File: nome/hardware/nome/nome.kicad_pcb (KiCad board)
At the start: 2 copper layers, 91.4 x 91.4 mm, 63 parts, among them J1 SJ-2524, J2 JTAG_SWD, J3 JST, J4 7SEG_DEBUG, SW1 SW_SPDT, SW2 Rotary_Encoder_Switch, U1 LM1117-1.8, U2 LM1117-3.3, U3 AS1115, U4 STMF411CEU6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

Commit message: Add metronome logo
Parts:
- added G***: LOGO, nome:metronome_logo, F.Cu at (90.4, 55.9)
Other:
- board text added: "NOME"
- board text added: "rev. A"
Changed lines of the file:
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@@
 (general
   (thickness 1.6)
-  (drawings 8)
+  (drawings 10)
   (tracks 937)
   (zones 0)
-  (modules 63)
+  (modules 64)
   (nets 107)
 )
@@
   (add_net +3V3)
 )
+  (module nome:metronome_logo (layer F.Cu)
+    (at 90.424 55.88)
+    (fp_text reference G*** (at 0 0) (layer F.SilkS) hide
+      (effects (font (thickness 0.3)))
+    )
+    (fp_text value LOGO (at 0.75 0) (layer F.SilkS) hide
+      (effects (font (thickness 0.3)))
+    )
+    (fp_poly (pts (xy 0.299212 -0.292148) (xy 0.233636 -0.169677) (xy 0.185654 -0.087032) (xy 0.149307 -0.036532)
+      (xy 0.118634 -0.010493) (xy 0.087674 -0.001233) (xy 0.072913 -0.000498) (xy 0 0)
+      (xy 0 -0.583298) (xy 0.452599 -0.583298) (xy 0.299212 -0.292148)) (layer F.SilkS) (width 0.01))
+    (fp_poly (pts (xy 2.59313 -0.961869) (xy 2.608985 -0.892796) (xy 2.630901 -0.784862) (xy 2.657712 -0.644817)
+      (xy 2.68825 -0.47941) (xy 2.721348 -0.295389) (xy 2.755838 -0.099504) (xy 2.790553 0.101496)
+      (xy 2.824326 0.300863) (xy 2.855989 0.491847) (xy 2.884375 0.667699) (xy 2.908317 0.821671)
+      (xy 2.926647 0.947014) (xy 2.938198 1.036978) (xy 2.941811 1.080428) (xy 2.943007 1.140084)
+      (xy 2.184533 1.140084) (xy 1.955859 1.139619) (xy 1.775596 1.138089) (xy 1.639137 1.135287)
+      (xy 1.541874 1.131009) (xy 1.479199 1.125051) (xy 1.446503 1.117207) (xy 1.439179 1.107272)
+      (xy 1.439302 1.106942) (xy 1.459766 1.06404) (xy 1.50165 0.982744) (xy 1.561826 0.86877)
+      (xy 1.637164 0.727837) (xy 1.724535 0.565661) (xy 1.820809 0.387959) (xy 1.922858 0.200449)
+      (xy 2.027552 0.008848) (xy 2.131761 -0.181127) (xy 2.232356 -0.363758) (xy 2.326208 -0.533328)
+      (xy 2.410188 -0.684121) (xy 2.481167 -0.810418) (xy 2.536014 -0.906502) (xy 2.5716 -0.966657)
+      (xy 2.584504 -0.985334) (xy 2.59313 -0.961869)) (layer F.SilkS) (width 0.01))
+    (fp_poly (pts (xy 0.615084 -6.781882) (xy 0.871614 -6.781131) (xy 1.099834 -6.779907) (xy 1.295607 -6.778237)
+      (xy 1.454793 -6.77615) (xy 1.573254 -6.773674) (xy 1.646851 -6.770837) (xy 1.671462 -6.767759)
+      (xy 1.675862 -6.738117) (xy 1.687978 -6.661689) (xy 1.706912 -6.544009) (xy 1.731765 -6.390615)
+      (xy 1.76164 -6.207041) (xy 1.795638 -5.998825) (xy 1.832862 -5.771502) (xy 1.853025 -5.648616)
+      (xy 1.89866 -5.36869) (xy 1.935741 -5.136227) (xy 1.964883 -4.946459) (xy 1.986699 -4.794621)
+      (xy 2.001804 -4.675946) (xy 2.010813 -4.585669) (xy 2.01434 -4.519022) (xy 2.013001 -4.471241)
+      (xy 2.008577 -4.442249) (xy 1.99512 -4.321577) (xy 1.999644 -4.171198) (xy 2.020312 -4.010591)
+      (xy 2.055292 -3.859236) (xy 2.066938 -3.822526) (xy 2.118092 -3.672129) (xy 1.362154 -2.26691)
+      (xy 1.226216 -2.014549) (xy 1.097316 -1.775905) (xy 0.977708 -1.555108) (xy 0.869648 -1.35629)
+      (xy 0.77539 -1.183582) (xy 0.697188 -1.041115) (xy 0.637298 -0.93302) (xy 0.597973 -0.863427)
+      (xy 0.581501 -0.836503) (xy 0.567022 -0.844537) (xy 0.55856 -0.899949) (xy 0.556785 -0.962442)
+      (xy 0.556785 -1.11357) (xy 0 -1.11357) (xy 0 -1.696868) (xy 0.556785 -1.696868)
+      (xy 0.556785 -2.253653) (xy 0 -2.253653) (xy 0 -2.836952) (xy 0.556785 -2.836952)
+      (xy 0.556785 -3.393737) (xy 0 -3.393737) (xy 0 -3.977035) (xy 0.556785 -3.977035)
+      (xy 0.556785 -4.507306) (xy 0 -4.507306) (xy 0 -5.090605) (xy 0.556785 -5.090605)
+      (xy 0.556785 -5.64739) (xy -1.11357 -5.64739) (xy -1.11357 -5.090605) (xy -0.556785 -5.090605)
+      (xy -0.556785 -4.507306) (xy -1.11357 -4.507306) (xy -1.11357 -3.977035) (xy -0.556785 -3.977035)
+      (xy -0.556785 -3.393737) (xy -1.11357 -3.393737) (xy -1.11357 -2.836952) (xy -0.556785 -2.836952)
+      (xy -0.556785 -2.253653) (xy -1.11357 -2.253653) (xy -1.11357 -1.696868) (xy -0.556785 -1.696868)
+      (xy -0.556785 -1.11357) (xy -1.11357 -1.11357) (xy -1.11357 -0.583298) (xy -0.556785 -0.583298)
+      (xy -0.556785 0) (xy -1.11357 0) (xy -1.11357 0.556785) (xy -0.556785 0.556785)
+      (xy -0.556785 1.140084) (xy -2.041544 1.140084) (xy -2.316596 1.139969) (xy -2.575099 1.139639)
+      (xy -2.812313 1.139114) (xy -3.023498 1.138416) (xy -3.203914 1.137566) (xy -3.348821 1.136585)
+      (xy -3.453476 1.135495) (xy -3.513141 1.134316) (xy -3.5256 1.133456) (xy -3.521328 1.106998)
+      (xy -3.508985 1.031062) (xy -3.489038 0.908507) (xy -3.461951 0.742188) (xy -3.42819 0.534965)
+      (xy -3.388222 0.289695) (xy -3.342512 0.009236) (xy -3.291526 -0.303556) (xy -3.23573 -0.645822)
+      (xy -3.175589 -1.014704) (xy -3.11157 -1.407344) (xy -3.044138 -1.820887) (xy -2.973758 -2.252472)
+      (xy -2.900898 -2.699243) (xy -2.880601 -2.823695) (xy -2.236306 -6.774217) (xy -0.282975 -6.781016)
+      (xy 0.033651 -6.781853) (xy 0.334384 -6.782132) (xy 0.615084 -6.781882)) (layer F.SilkS) (width 0.01))
+    (fp_poly (pts (xy 3.722894 -5.473828) (xy 3.781092 -5.445337) (xy 3.86248 -5.403449) (xy 3.955472 -5.354338)
+      (xy 4.048485 -5.304177) (xy 4.129934 -5.259141) (xy 4.188234 -5.225402) (xy 4.211019 -5.210136)
+      (xy 4.205238 -5.182799) (xy 4.179181 -5.12099) (xy 4.138052 -5.036743) (xy 4.126115 -5.01376)
+      (xy 4.029223 -4.829373) (xy 4.106328 -4.714738) (xy 4.184826 -4.572561) (xy 4.228003 -4.424615)
+      (xy 4.240216 -4.253431) (xy 4.238056 -4.186225) (xy 4.203087 -3.973776) (xy 4.124304 -3.788483)
+      (xy 4.005494 -3.634137) (xy 3.850442 -3.514527) (xy 3.662937 -3.433443) (xy 3.447155 -3.394702)
+      (xy 3.248694 -3.38048) (xy 1.890788 -0.861691) (xy 1.708097 -0.522657) (xy 1.532607 -0.196678)
+      (xy 1.365946 0.113206) (xy 1.20974 0.40396) (xy 1.065615 0.672544) (xy 0.935198 0.915921)
+      (xy 0.820115 1.131054) (xy 0.721993 1.314904) (xy 0.642457 1.464434) (xy 0.583135 1.576606)
+      (xy 0.545653 1.648382) (xy 0.531637 1.676725) (xy 0.531577 1.676984) (xy 0.556963 1.680977)
+      (xy 0.630229 1.684703) (xy 0.746226 1.688079) (xy 0.899808 1.691025) (xy 1.085826 1.693458)
+      (xy 1.299134 1.695297) (xy 1.534583 1.696462) (xy 1.787027 1.696869) (xy 3.044848 1.696869)
+      (xy 3.059928 1.769781) (xy 3.06879 1.818361) (xy 3.084811 1.912235) (xy 3.107145 2.046127)
+      (xy 3.134944 2.214758) (xy 3.167359 2.412852) (xy 3.203544 2.63513) (xy 3.24265 2.876315)
+      (xy 3.283831 3.131129) (xy 3.326238 3.394296) (xy 3.369025 3.660536) (xy 3.411343 3.924574)
+      (xy 3.452345 4.18113) (xy 3.491184 4.424928) (xy 3.527011 4.650689) (xy 3.558979 4.853137)
+      (xy 3.586241 5.026994) (xy 3.60795 5.166981) (xy 3.623256 5.267822) (xy 3.631314 5.324239)
+      (xy 3.632359 5.334136) (xy 3.630835 5.34067) (xy 3.62459 5.346585) (xy 3.611114 5.351912)
+      (xy 3.587898 5.356681) (xy 3.552433 5.360924) (xy 3.50221 5.36467) (xy 3.434719 5.367951)
+      (xy 3.347452 5.370798) (xy 3.237898 5.373241) (xy 3.10355 5.37531) (xy 2.941896 5.377038)
+      (xy 2.750429 5.378454) (xy 2.52664 5.379589) (xy 2.268018 5.380474) (xy 1.972054 5.381139)
+      (xy 1.63624 5.381616) (xy 1.258066 5.381936) (xy 0.835022 5.382128) (xy 0.3646 5.382224)
+      (xy -0.155709 5.382254) (xy -0.294523 5.382255) (xy -4.221406 5.382255) (xy -4.207556 5.3226)
+      (xy -4.20108 5.286858) (xy -4.186922 5.203198) (xy -4.165805 5.076058) (xy -4.138456 4.909877)
+      (xy -4.1056 4.709092) (xy -4.067963 4.478141) (xy -4.026269 4.221464) (xy -3.981243 3.943497)
+      (xy -3.933613 3.648679) (xy -3.906404 3.479938) (xy -3.619102 1.696932) (xy -1.89253 1.6969)
+      (xy -0.165959 1.696869) (xy 1.280413 -0.989497) (xy 2.726784 -3.675862) (xy 2.633947 -3.859591)
+      (xy 2.588201 -3.95392) (xy 2.56131 -4.026589) (xy 2.549096 -4.09796) (xy 2.547377 -4.188397)
+      (xy 2.549972 -4.268684) (xy 2.570192 -4.458233) (xy 2.618179 -4.613947) (xy 2.699852 -4.750308)
+      (xy 2.787044 -4.848864) (xy 2.947739 -4.976218) (xy 3.128056 -5.05485) (xy 3.316737 -5.085993)
+      (xy 3.491615 -5.096127) (xy 3.592678 -5.285589) (xy 3.640222 -5.374372) (xy 3.677299 -5.442951)
+      (xy 3.697613 -5.479703) (xy 3.699471 -5.482749) (xy 3.722894 -5.473828)) (layer F.SilkS) (width 0.01))
+    (fp_poly (pts (xy 3.685387 6.787474) (xy 2.253654 6.787474) (xy 2.253654 5.93904) (xy 3.685387 5.93904)
+      (xy 3.685387 6.787474)) (layer F.SilkS) (width 0.01))
+    (fp_poly (pts (xy -2.810438 6.787474) (xy -4.242171 6.787474) (xy -4.242171 5.93904) (xy -2.810438 5.93904)
+      (xy -2.810438 6.787474)) (layer F.SilkS) (width 0.01))
+  )
   (module Connectors:1pin (layer F.Cu)
     (at 106.172 96.012)
@@
     )
   )
+  (gr_text "rev. A" (at 36.068 60.452) (layer F.SilkS)
+    (effects (font (size 1.5 1.5) (thickness 0.3)))
+  )
+  (gr_text NOME (at 38.608 57.404) (layer F.SilkS)
+    (effects (font (size 3 3) (thickness 0.3)))
+  )
   (gr_line (start 48.26 129.54) (end 20.32 101.6) (layer Edge.Cuts) (width 0.1))

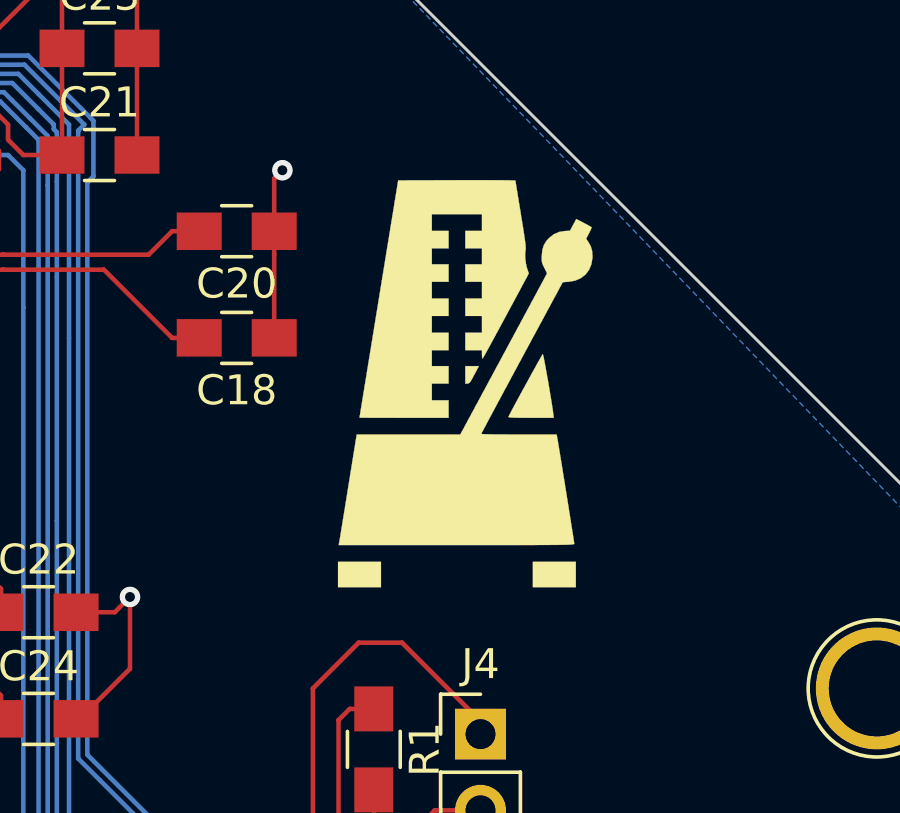
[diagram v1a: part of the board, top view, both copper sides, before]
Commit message: Move logo over
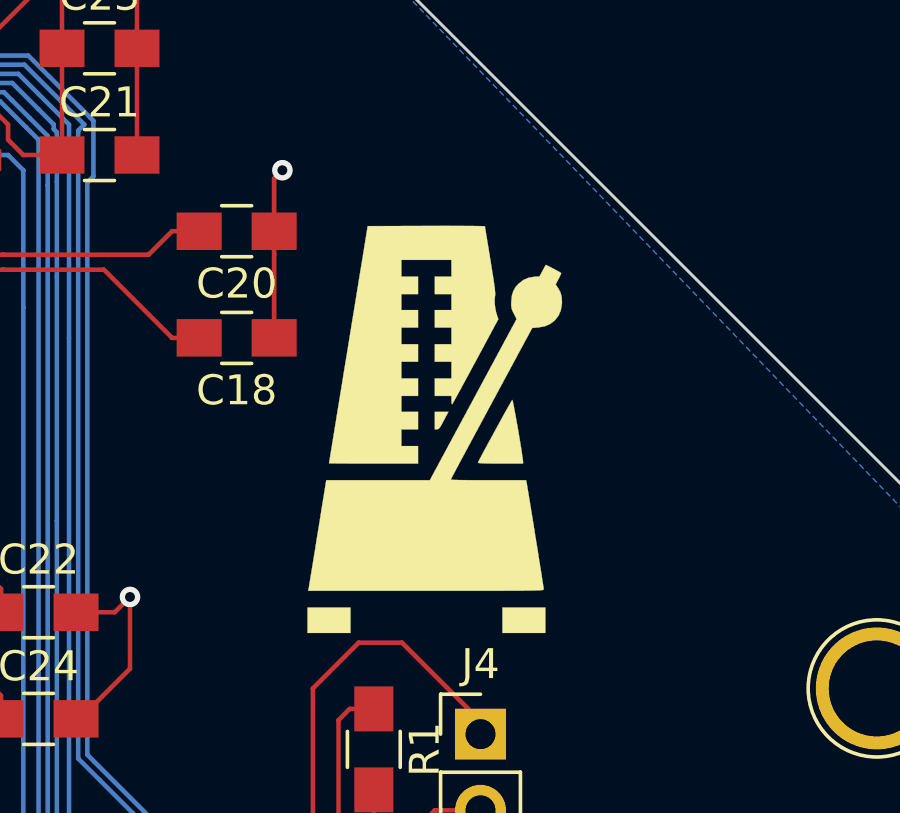
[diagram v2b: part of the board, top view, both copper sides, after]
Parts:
- moved G*** 1.83 mm to (89.4, 57.4)
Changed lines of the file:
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@@
 )
   (module nome:metronome_logo (layer F.Cu)
-    (at 90.424 55.88)
+    (at 89.408 57.404)
     (fp_text reference G*** (at 0 0) (layer F.SilkS) hide
       (effects (font (thickness 0.3)))
